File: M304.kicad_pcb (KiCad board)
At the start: 2 copper layers, 101.6 x 53.3 mm, 70 parts, among them J1 LCD 2004, J2 Relay OUT, J3 iM920, J4 GPS, P1 Digital, P10 CONN_01X01, P11 CONN_01X01, P12 CONN_01X01, P13 CONN_01X01, P2 Power, P3 Analog, P4 Analog, P5 PWM, P6 PWM, P7 Communication, P8 CONN_01X01, P9 CONN_01X01, U1 DS1307+, U2 24LC256, U3 W5500

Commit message: 大修正
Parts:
- added C1: 0.1uF, Capacitor_THT:C_Disc_D3.0mm_W2.0mm_P2.50mm, F.Cu at (228.9, 104.4)
- added C2: 0.1uF, Capacitor_THT:C_Disc_D3.0mm_W2.0mm_P2.50mm, F.Cu at (234.5, 104.4)
- added C3: 100u/25V, Capacitor_THT:CP_Radial_D5.0mm_P2.00mm, F.Cu at (229.6, 99.3)
- added J5: Conn_01x02, Connector_JST:JST_VH_B2P-VH_1x02_P3.96mm_Vertical, F.Cu at (220.3, 100.8)
- added R1: 10k, Resistor_THT:R_Axial_DIN0207_L6.3mm_D2.5mm_P7.62mm_Horizontal, F.Cu at (228.9, 130.0)
- added R2: 10k, Resistor_THT:R_Axial_DIN0207_L6.3mm_D2.5mm_P7.62mm_Horizontal, F.Cu at (228.9, 138.1)
- added R3: 10k, Resistor_THT:R_Axial_DIN0207_L6.3mm_D2.5mm_P7.62mm_Horizontal, F.Cu at (239.6, 130.0)
- added R4: 10k, Resistor_THT:R_Axial_DIN0207_L6.3mm_D2.5mm_P7.62mm_Horizontal, F.Cu at (239.6, 138.1)
- added R5: 10k, Resistor_THT:R_Axial_DIN0207_L6.3mm_D2.5mm_P7.62mm_Horizontal, F.Cu at (239.6, 134.1)
- added R6: 10k, Resistor_THT:R_Axial_DIN0207_L6.3mm_D2.5mm_P7.62mm_Horizontal, F.Cu at (228.9, 134.1)
- added RV1: B10k, Potentiometer_THT:Potentiometer_Runtron_RM-065_Vertical, F.Cu at (246.1, 178.3)
- added RV2: B10k, Potentiometer_THT:Potentiometer_Alps_RK09K_Single_Vertical, F.Cu at (230.8, 180.9)
- added RV2: B10k, Potentiometer_THT:Potentiometer_Alps_RK09K_Single_Vertical, F.Cu at (210.3, 181.4)
- added SW1: RESET, HOLLY:TVDT18-050, F.Cu at (221.7, 117.3)
- added SW2: SW_A, HOLLY:TVDT18-050, F.Cu at (226.3, 166.6)
- added SW3: SW_B, HOLLY:TVDT18-050, F.Cu at (226.3, 159.5)
- added SW4: SW_C, HOLLY:TVDT18-050, F.Cu at (234.3, 166.6)
- added SW5: SW_D, HOLLY:TVDT18-050, F.Cu at (234.3, 159.5)
- added Y1: 32.768kHz, Crystal:Crystal_C26-LF_D2.1mm_L6.5mm_Horizontal, F.Cu at (219.0, 157.3)
- U1: footprint Package_DIP:DIP-8_W7.62mm -> Package_DIP:DIP-8_W7.62mm_LongPads

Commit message: PCB layout
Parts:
- removed the RV2 at (230.8, 180.9)
- added REF**: MountingHole_4.3mm_M4, MountingHole:MountingHole_4.3mm_M4, F.Cu at (253.7, 50.2)
- added REF**: MountingHole_4.3mm_M4, MountingHole:MountingHole_4.3mm_M4, F.Cu at (96.2, 50.2)
- added REF**: MountingHole_4.3mm_M4, MountingHole:MountingHole_4.3mm_M4, F.Cu at (253.7, 205.1)
- added REF**: MountingHole_4.3mm_M4, MountingHole:MountingHole_4.3mm_M4, F.Cu at (96.2, 205.1)
- J1: footprint Connector_PinHeader_2.54mm:PinHeader_1x16_P2.54mm_Vertical -> Connector_PinSocket_2.54mm:PinSocket_1x16_P2.54mm_Vertical
- P2: footprint Socket_Arduino_Mega:Socket_Strip_Arduino_1x08 -> Connector_PinHeader_2.54mm:PinHeader_1x08_P2.54mm_Vertical; moved to B.Cu
- P3, P4, P5, P6, P7: moved to B.Cu
- moved RV1 182.0 mm to (111.4, 55.9)
- moved C3 141.7 mm to (97.1, 149.4)
- moved J5 130.2 mm to (94.8, 135.3)
- moved SW2 94.0 mm to (216.9, 73.1)
- moved SW3 94.0 mm to (216.9, 66.0)
- moved SW4 94.0 mm to (224.9, 73.1)
- moved SW5 94.0 mm to (224.9, 66.0)
- moved J1 87.8 mm to (122.2, 47.8), turned to 90 degrees
- moved P1 5.68 mm to (195.0, 108.9)
- moved P10 5.68 mm to (197.5, 114.0)
- moved P13 5.68 mm to (191.2, 65.7)
- moved P2 5.68 mm to (128.9, 114.0), turned to -90 degrees
- moved P3 5.68 mm to (151.8, 114.0)
- moved P4 5.68 mm to (174.7, 114.0)
- moved P5 5.68 mm to (119.8, 65.7)
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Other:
- board size 101.6 x 53.3 mm -> 170.7 x 170 mm

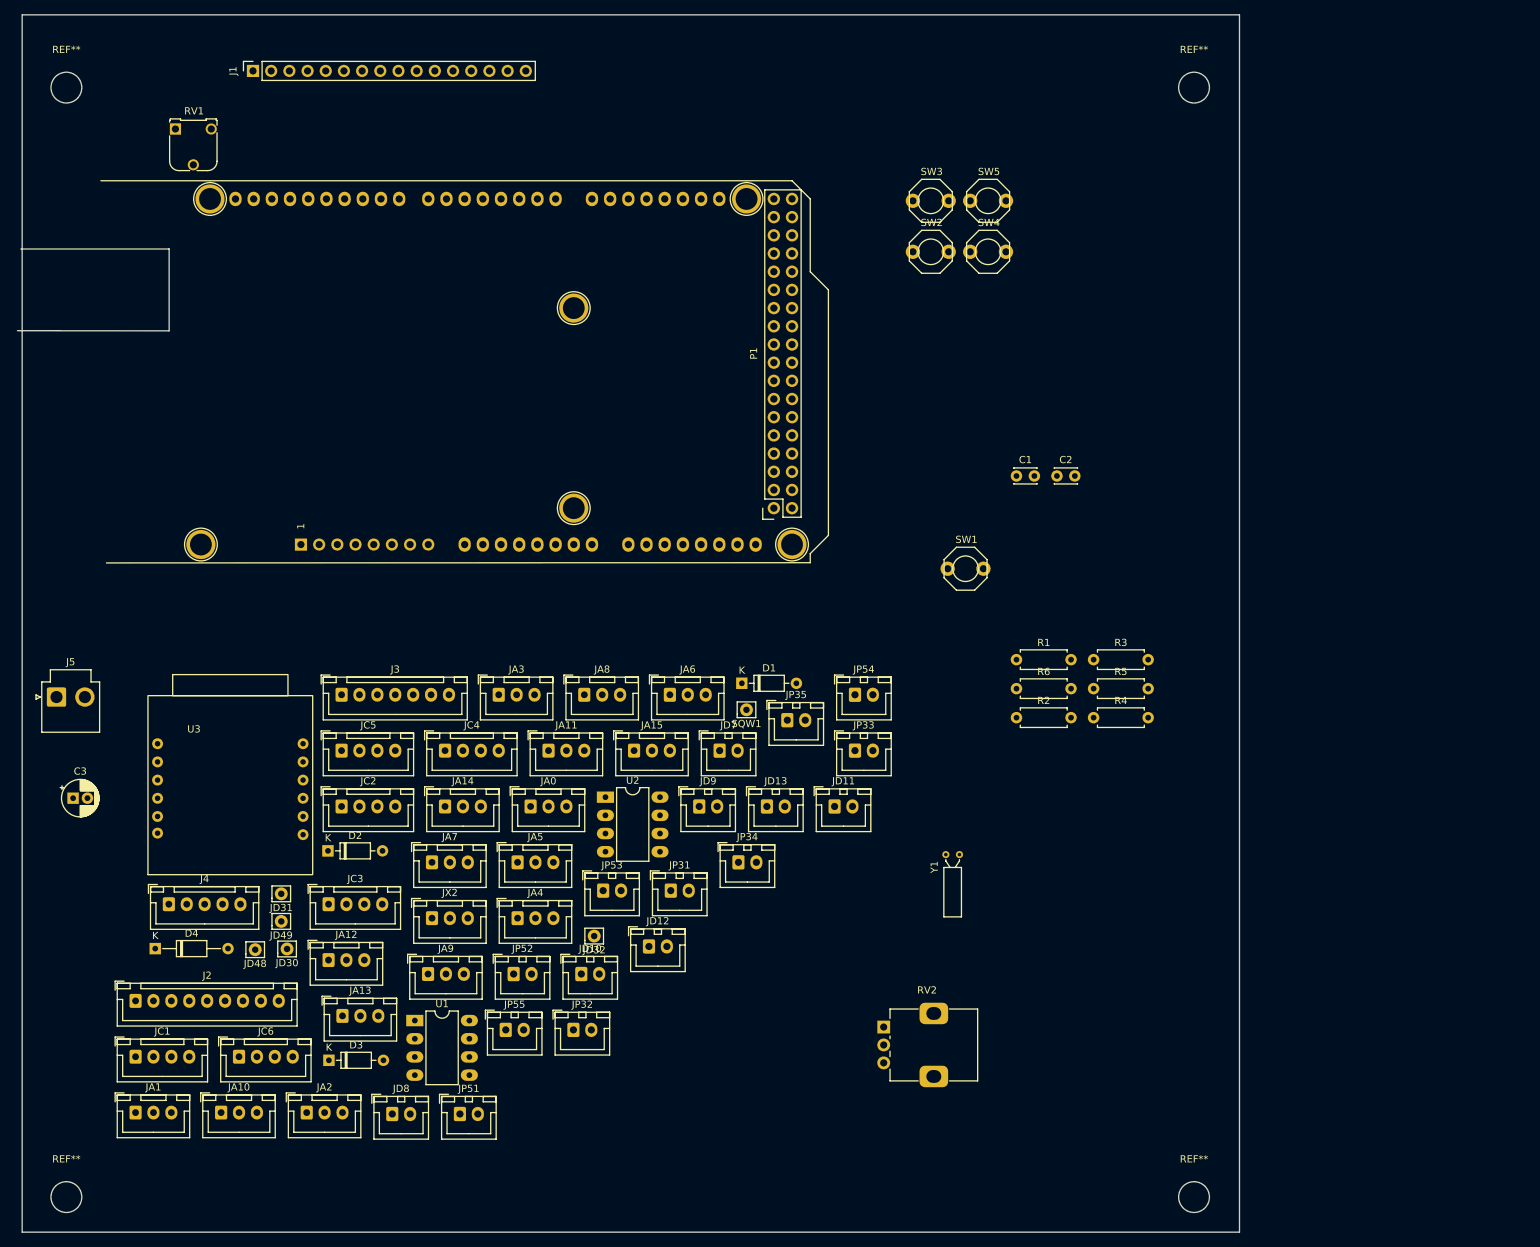
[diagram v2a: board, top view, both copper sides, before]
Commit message: Arduino MEGA pin direction change
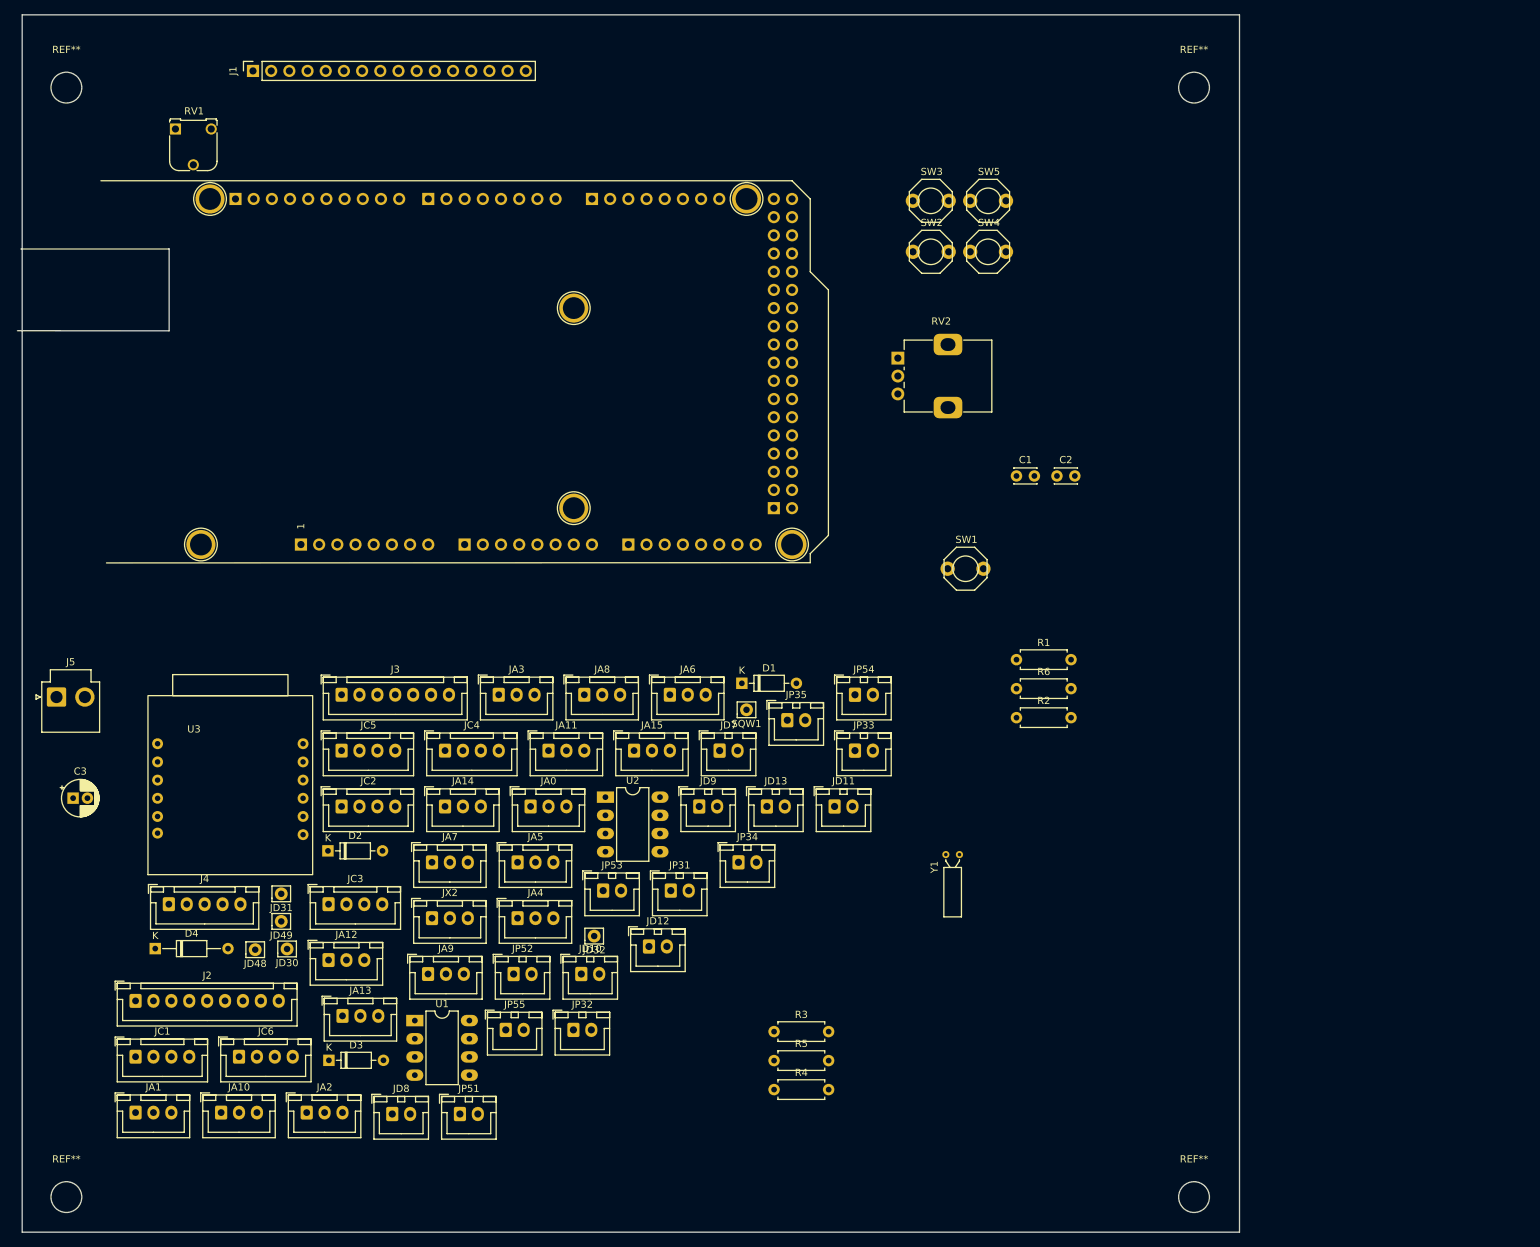
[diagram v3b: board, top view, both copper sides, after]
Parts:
- P1: footprint Socket_Arduino_Mega:Socket_Strip_Arduino_2x18 -> Connector_PinHeader_2.54mm:PinHeader_2x18_P2.54mm_Vertical; moved to B.Cu
- P3, P4, P6, P7: footprint Socket_Arduino_Mega:Socket_Strip_Arduino_1x08 -> Connector_PinHeader_2.54mm:PinHeader_1x08_P2.54mm_Vertical
- P5: footprint Socket_Arduino_Mega:Socket_Strip_Arduino_1x10 -> Connector_PinHeader_2.54mm:PinHeader_1x10_P2.54mm_Vertical
- moved RV2 93.4 mm to (212.3, 87.9)
- moved R3 68.5 mm to (195.0, 182.0)
- moved R4 68.5 mm to (195.0, 190.1)
- moved R5 68.5 mm to (195.0, 186.0)
- turned P1 to 0 degrees
- turned P3 to -90 degrees
- turned P4 to -90 degrees
- turned P5 to -90 degrees
- turned P6 to -90 degrees
- turned P7 to -90 degrees

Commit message: PCB Design start
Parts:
- added BT1: CR2032, Akizuki:CH74-2032LF, F.Cu at (94.0, 66.0)
- added D2-1: LED, LED_THT:LED_D3.0mm, F.Cu at (195.6, 197.5)
- added D2-2: LED, LED_THT:LED_D3.0mm, F.Cu at (195.6, 188.6)
- added D2-3: 1N4148, Diode_THT:D_DO-35_SOD27_P7.62mm_Horizontal, F.Cu at (193.0, 172.7)
- added R2-1: 510, Resistor_THT:R_Axial_DIN0207_L6.3mm_D2.5mm_P7.62mm_Horizontal, F.Cu at (203.2, 189.9)
- added R2-2: 510, Resistor_THT:R_Axial_DIN0207_L6.3mm_D2.5mm_P7.62mm_Horizontal, F.Cu at (194.3, 182.2)
- added R2-3: 510, Resistor_THT:R_Axial_DIN0207_L6.3mm_D2.5mm_P7.62mm_Horizontal, F.Cu at (201.9, 177.2)
- added RN2-1: 2.2k, Resistor_THT:R_Array_SIP9, F.Cu at (208.9, 158.7)
- added RN2-2: 2.2k, Resistor_THT:R_Array_SIP9, F.Cu at (208.9, 184.8)
- added U2-1: TLP222G-2, Akizuki:TLP222A-2, F.Cu at (235.6, 162.6)
- added U2-2: TLP222G-2, Akizuki:TLP222A-2, F.Cu at (235.6, 175.9)
- added U2-3: TLP222G-2, Akizuki:TLP222A-2, F.Cu at (235.6, 189.2)
- added U2-4: TLP222G-2, Akizuki:TLP222A-2, F.Cu at (235.6, 202.6)
- added U2-5: TLP222G-2, Akizuki:TLP222A-2, F.Cu at (222.2, 162.6)
- added U2-6: TLP222G-2, Akizuki:TLP222A-2, F.Cu at (222.2, 175.9)
- added U2-7: TLP222G-2, Akizuki:TLP222A-2, F.Cu at (222.2, 189.2)
- added U2-8: TLP222G-2, Akizuki:TLP222A-2, F.Cu at (222.2, 202.6)
- J5: value Conn_01x02 -> POWER IN
- moved J4 148.2 mm to (252.0, 120.1), turned to -90 degrees
- moved J2 146.6 mm to (252.0, 165.9), turned to -90 degrees
- moved Y1 124.5 mm to (124.3, 76.5), turned to -90 degrees
- moved J3 117.6 mm to (252.1, 140.3), turned to -90 degrees
- moved JP33 111.7 mm to (99.1, 174.0), turned to 180 degrees
- moved JP35 111.4 mm to (99.1, 191.8), turned to 180 degrees
- moved D2 107.0 mm to (234.3, 123.2)
- moved JP54 106.0 mm to (111.8, 182.9), turned to 180 degrees
- moved U1 105.5 mm to (128.9, 76.2)
- moved D3 105.3 mm to (231.8, 149.9)
- moved C2 104.3 mm to (131.3, 89.4)
- moved C1 100.1 mm to (134.0, 72.4), turned to 180 degrees
- moved R3 98.0 mm to (148.3, 95.8)
- moved SQW1 94.3 mm to (113.3, 83.8)
- moved JP34 94.2 mm to (99.1, 182.9), turned to 180 degrees
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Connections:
- C1 pad 2: SDA -> GND
- C2 pad 1: +5V -> GND
- C2 pad 2: SDA -> +5V
- C3 pad 2: SDA -> GND
- J1 pad 1: SDA -> GND
- J1 pad 16: SDA -> GND
- J2 pad 1: /22 -> /Relay Manual Switch/OUTPUT1
- J2 pad 2: /23 -> /Relay Manual Switch/OUTPUT2
- J2 pad 3: /24 -> /Relay Manual Switch/OUTPUT3
- J2 pad 4: /25 -> /Relay Manual Switch/OUTPUT4
- J2 pad 5: /26 -> /Relay Manual Switch/OUTPUT5
- J2 pad 6: /27 -> /Relay Manual Switch/OUTPUT6
- J2 pad 7: /28 -> /Relay Manual Switch/OUTPUT7
- J2 pad 8: /29 -> /Relay Manual Switch/OUTPUT8
- J3 pad 3: SDA -> GND
- J4 pad 4: SDA -> GND
- J5 pad 1: SDA -> GND
- JA0 pad 1: SDA -> GND
- JA0 pad 3: +5V -> +3V3
- JA1 pad 1: SDA -> GND
- JA1 pad 3: +5V -> +3V3
- JA10 pad 1: SDA -> GND
- JA11 pad 1: SDA -> GND
- JA12 pad 1: SDA -> GND
- JA13 pad 1: SDA -> GND
- JA14 pad 1: SDA -> GND
- JA15 pad 1: SDA -> GND
- JA2 pad 1: SDA -> GND
- JA2 pad 3: +5V -> +3V3
- JA3 pad 1: SDA -> GND
- JA3 pad 3: +5V -> +3V3
- JA4 pad 1: SDA -> GND
- JA4 pad 3: +5V -> +3V3
- JA5 pad 1: SDA -> GND
- JA5 pad 3: +5V -> +3V3
- JA6 pad 1: SDA -> GND
- JA6 pad 3: +5V -> +3V3
- JA7 pad 1: SDA -> GND
- JA7 pad 3: +5V -> +3V3
- JA8 pad 1: SDA -> GND
- JA9 pad 1: SDA -> GND
- JC1 pad 1: SDA -> GND
- JC2 pad 1: SDA -> GND
- JC3 pad 1: SDA -> GND
- JC4 pad 1: SDA -> GND
- JC5 pad 1: SDA -> GND
- JC6 pad 1: SDA -> GND
- JD10 pad 1: SDA -> GND
- JD11 pad 1: SDA -> GND
- JD12 pad 1: SDA -> GND
- JD13 pad 1: SDA -> GND
- JD7 pad 1: SDA -> GND
- JD8 pad 1: SDA -> GND
- JD9 pad 1: SDA -> GND
- JP31 pad 1: SDA -> GND
- JP32 pad 1: SDA -> GND
- JP33 pad 1: SDA -> GND
- JP34 pad 1: SDA -> GND
- JP35 pad 1: SDA -> GND
- JP51 pad 1: SDA -> GND
- JP52 pad 1: SDA -> GND
- JP53 pad 1: SDA -> GND
- JP54 pad 1: SDA -> GND
- JP55 pad 1: SDA -> GND
- JX2 pad 1: SDA -> GND
- P1 pad 1: SDA -> GND
- P1 pad 2: SDA -> GND
- P2 pad 6: SDA -> GND
- P2 pad 7: SDA -> GND
- P5 pad 4: SDA -> GND
- RV1 pad 1: SDA -> GND
- RV2 pad 1: SDA -> GND
- RV2 pad MP: SDA -> GND
- SW1 pad 2: SDA -> GND
- SW2 pad 1: SDA -> GND
- SW3 pad 1: SDA -> GND
- SW4 pad 1: SDA -> GND
- SW5 pad 1: SDA -> GND
- U1 pad 4: SDA -> GND
- U2 pad 1: SDA -> GND
- U2 pad 2: SDA -> GND
- U2 pad 3: SDA -> GND
- U2 pad 4: SDA -> GND
- U2 pad 7: SDA -> GND
- U3 pad 1: SDA -> GND
- U3 pad 12: SDA -> GND
- U3 pad 2: SDA -> GND
- Y1 pad 1: Net-(U1-Pad2) -> Net-(U1-Pad1)
- Y1 pad 2: Net-(U1-Pad1) -> Net-(U1-Pad2)
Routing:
- net +5V: track 0.00 -> 578.3 mm
- net +3V3: track 0.00 -> 180.1 mm
- net SCL: track 0.00 -> 145.3 mm, vias 0 -> 3
- net SDA: track 0.00 -> 140.0 mm, vias 0 -> 1
- net Net-(BT1-Pad1): track 0.00 -> 51.4 mm
- net Net-(SQW1-Pad1): track 0.00 -> 30.7 mm, vias 0 -> 1
- net /V0: track 0.00 -> 28.2 mm
- net Net-(D4-Pad2): track 0.00 -> 7.32 mm
- net Net-(U1-Pad2): track 0.00 -> 4.76 mm
- net Net-(U1-Pad1): track 0.00 -> 4.75 mm
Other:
- board text added: "3.3V"
- board text added: "5V"

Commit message: PCB Design cont.
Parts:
- added SW6: SW_ENTER, HOLLY:TVDT18-050, F.Cu at (238.8, 66.0)
- moved SQW1 32.5 mm to (145.4, 78.7)
- moved SW2 27.8 mm to (238.8, 55.9), turned to 180 degrees
- moved SW3 24.1 mm to (238.8, 76.2), turned to 180 degrees
- moved SW5 24.0 mm to (248.9, 66.0), turned to 180 degrees
- moved SW4 7.97 mm to (228.6, 66.0), turned to 180 degrees
- moved R1 7.95 mm to (131.4, 109.2)
- moved RV2 7.44 mm to (241.3, 86.7), turned to -90 degrees
- moved JA5 2.58 mm to (132.0, 173.2)
- moved JA0 2.54 mm to (132.0, 128.8)
- moved JA2 2.54 mm to (132.0, 146.6)
- moved JA3 2.54 mm to (132.0, 155.5)
- moved JA4 2.54 mm to (132.0, 164.4)
- moved JA6 2.54 mm to (132.0, 182.1)
- moved JA7 2.50 mm to (132.1, 191.1)
- moved JA1 2.50 mm to (132.0, 137.7)
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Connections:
- R1 pad 1: +5V -> /Reset
- R1 pad 2: /Reset -> +5V
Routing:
- net /13(**): track 0.00 -> 213.8 mm
- net /12(**): track 0.00 -> 208.7 mm
- net /A7: track 0.00 -> 109.0 mm
- net /A6: track 0.00 -> 98.6 mm
- net /A5: track 0.00 -> 87.5 mm
- net /A15: track 0.00 -> 80.6 mm, vias 0 -> 3
- net /A4: track 0.00 -> 76.5 mm
- net /A3: track 0.00 -> 66.5 mm
- net /A2: track 0.00 -> 55.5 mm
- net +5V: track 578.3 -> 624.0 mm, vias 0 -> 1
- net /A1: track 0.00 -> 44.8 mm
- net /Reset: track 0.00 -> 43.8 mm, vias 0 -> 1
- net /A0: track 0.00 -> 33.4 mm
- net Net-(SQW1-Pad1): track 30.7 -> 8.91 mm, vias 1 -> 0
- net SCL: track 145.3 -> 137.8 mm
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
